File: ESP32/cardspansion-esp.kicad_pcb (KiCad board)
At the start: 2 copper layers, 22 x 30 mm, 5 parts, among them J1 M2-E 2230, Y1 ASE-32.768KHZ

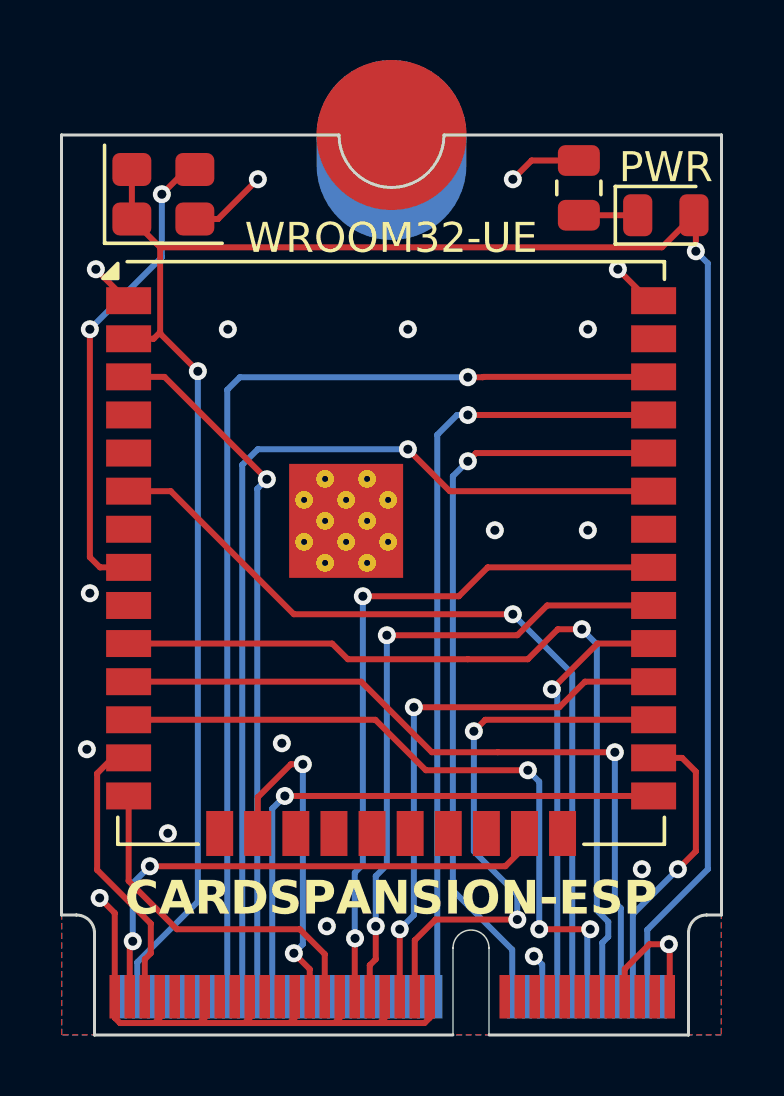
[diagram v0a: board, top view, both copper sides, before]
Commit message: Fix cardspansion-esp I2S wiring
I2S-SDIN and I2S-SDOUT nets were switched around
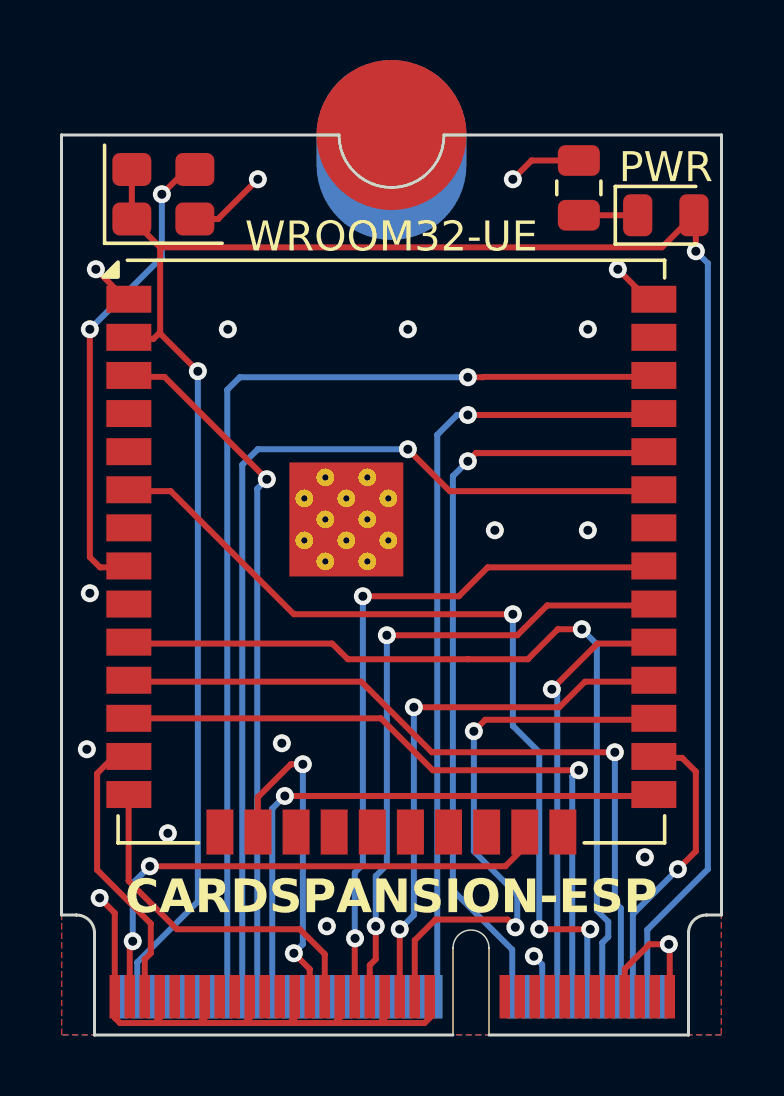
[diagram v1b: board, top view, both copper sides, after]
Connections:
- J1 pad 12: /I2S-SDOUT -> /I2S-SDIN
- J1 pad 14: /I2S-SDIN -> /I2S-SDOUT
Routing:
- net /I2S-SDIN: track 28.1 -> 29.4 mm, vias 1 -> 3
- net /I2S-SDOUT: track 23.5 -> 23.4 mm, vias 3 -> 1
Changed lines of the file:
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@@
 	(footprint "RF_Module:ESP32-WROOM-32UE"
 		(layer "F.Cu")
-		(at 28.4425 38.4575)
+		(at 28.45 38.41)
 		(descr "2.4 GHz Wi-Fi and Bluetooth module, https://www.espressif.com/sites/default/files/documentation/esp32-wroom-32e_esp32-wroom-32ue_datasheet_en.pdf")
 		(tags "2.4 GHz Wi-Fi and Bluetooth module")
@@
 		(sheetname "/")
 		(sheetfile "cardspansion-esp.kicad_sch")
+		(clearance 0.1)
 		(attr smd)
 		(fp_line
@@
 			(layer "F.Fab")
 		)
+		(fp_text user "${REFERENCE}"
+			(at 0 0 0)
+			(unlocked yes)
+			(layer "F.Fab")
+			(effects
+				(font
+					(size 1 1)
+					(thickness 0.15)
+				)
+			)
+		)
 		(pad "1" smd rect
 			(at -8.75 -8.41)
@@
 			(size 0.35 1.45)
 			(layers "B.Cu" "B.Mask")
-			(net 24 "/I2S-SDOUT")
+			(net 55 "/I2S-SDIN")
 			(pinfunction "PCM_IN/I2S_SD_IN")
 			(pintype "input")
@@
 			(size 0.35 1.45)
 			(layers "B.Cu" "B.Mask")
-			(net 55 "/I2S-SDIN")
+			(net 24 "/I2S-SDOUT")
 			(pinfunction "PCM_OUT/I2S_SD_OUT")
 			(pintype "output")
@@
 	)
 	(via
-		(at 36.8 49)
+		(at 18.3 45)
 		(size 0.6)
 		(drill 0.3)
@@
 	)
 	(via
-		(at 18.3 45)
+		(at 36.9 48.6)
 		(size 0.6)
 		(drill 0.3)
@@
 	)
 	(segment
-		(start 27.9175 44.0175)
-		(end 19.6925 44.0175)
-		(width 0.2)
-		(layer "F.Cu")
-		(net 24)
-	)
-	(segment
-		(start 33 45.7)
-		(end 29.6 45.7)
+		(start 29.8329 45.7)
+		(end 34.7 45.7)
 		(width 0.2)
 		(layer "F.Cu")
@@
 	)
 	(segment
-		(start 33.38 51)
-		(end 35.08 51)
+		(start 19.7 43.97)
+		(end 28.1029 43.97)
 		(width 0.2)
 		(layer "F.Cu")
@@
 	)
 	(segment
-		(start 29.6 45.7)
-		(end 27.9175 44.0175)
+		(start 28.1029 43.97)
+		(end 29.8329 45.7)
 		(width 0.2)
 		(layer "F.Cu")
@@
 	)
 	(via
-		(at 33 45.7)
-		(size 0.6)
-		(drill 0.3)
-		(layers "F.Cu" "B.Cu")
-		(net 24)
-	)
-	(via
-		(at 33.38 51)
-		(size 0.6)
-		(drill 0.3)
-		(layers "F.Cu" "B.Cu")
-		(net 24)
-	)
-	(via
-		(at 35.08 51)
+		(at 34.7 45.7)
 		(size 0.6)
 		(drill 0.3)
@@
 	)
 	(segment
-		(start 33.38 51)
-		(end 33.38 46.08)
-		(width 0.2)
-		(layer "B.Cu")
-		(net 24)
-	)
-	(segment
-		(start 33.38 46.08)
-		(end 33 45.7)
+		(start 34.7 45.7)
+		(end 34.68 45.7)
 		(width 0.2)
 		(layer "B.Cu")
@@
 	)
 	(segment
-		(start 35.08 51)
-		(end 34.98 51.1)
+		(start 34.68 45.7)
+		(end 34.48 45.9)
 		(width 0.2)
 		(layer "B.Cu")
@@
 	)
 	(segment
-		(start 34.98 51.1)
-		(end 34.98 53.25)
+		(start 34.48 45.9)
+		(end 34.48 53.25)
 		(width 0.2)
 		(layer "B.Cu")
@@
 	(segment
 		(start 29.8 45.1)
-		(end 32 45.1)
-		(width 0.2)
-		(layer "F.Cu")
-		(net 49)
-	)
-	(segment
-		(start 19.6925 42.7475)
-		(end 27.4475 42.7475)
+		(end 35.9 45.1)
 		(width 0.2)
 		(layer "F.Cu")
@@
 	)
 	(segment
-		(start 28.3 43.6)
+		(start 27.4475 42.7475)
 		(end 29.8 45.1)
 		(width 0.2)
@@
 	)
 	(segment
-		(start 32 45.1)
-		(end 35.9 45.1)
-		(width 0.2)
-		(layer "F.Cu")
-		(net 49)
-	)
-	(segment
-		(start 27.4475 42.7475)
-		(end 28.3 43.6)
+		(start 19.6925 42.7475)
+		(end 27.4475 42.7475)
 		(width 0.2)
 		(layer "F.Cu")
@@
 	)
 	(segment
-		(start 29.23 51.37)
-		(end 29.23 53.25)
+		(start 32.325616 50.677087)
+		(end 29.922913 50.677087)
+		(width 0.2)
+		(layer "F.Cu")
+		(net 53)
+	)
+	(segment
+		(start 32.582711 50.934182)
+		(end 32.325616 50.677087)
 		(width 0.2)
 		(layer "F.Cu")
@@
 	(segment
 		(start 29.922913 50.677087)
-		(end 32.648064 50.677087)
+		(end 29.23 51.37)
 		(width 0.2)
 		(layer "F.Cu")
@@
 	(segment
 		(start 29.23 51.37)
-		(end 29.922913 50.677087)
+		(end 29.23 53.25)
 		(width 0.2)
 		(layer "F.Cu")
@@
 	)
 	(via
-		(at 32.648064 50.677087)
+		(at 32.582711 50.934182)
 		(size 0.6)
 		(drill 0.3)
@@
 	)
 	(segment
-		(start 32.648064 50.677087)
+		(start 32.648064 50.868829)
 		(end 32.648064 49.848064)
 		(width 0.2)
@@
 	)
 	(segment
+		(start 32.582711 50.934182)
+		(end 32.648064 50.868829)
+		(width 0.2)
+		(layer "B.Cu")
+		(net 53)
+	)
+	(segment
 		(start 32.5 40.5)
 		(end 25.2 40.5)
@@
 	)
 	(segment
+		(start 33.38 51)
+		(end 35.08 51)
+		(width 0.2)
+		(layer "F.Cu")
+		(net 55)
+	)
+	(segment
 		(start 25.2 40.5)
 		(end 21.0975 36.3975)
@@
 		(net 55)
 	)
+	(via
+		(at 33.38 51)
+		(size 0.6)
+		(drill 0.3)
+		(layers "F.Cu" "B.Cu")
+		(net 55)
+	)
+	(via
+		(at 35.08 51)
+		(size 0.6)
+		(drill 0.3)
+		(layers "F.Cu" "B.Cu")
+		(net 55)
+	)
+	(segment
+		(start 33.38 45.1)
+		(end 33.38 51)
+		(width 0.2)
+		(layer "B.Cu")
+		(net 55)
+	)
+	(segment
+		(start 35.08 51)
+		(end 34.98 51.1)
+		(width 0.2)
+		(layer "B.Cu")
+		(net 55)
+	)
+	(segment
+		(start 34.98 51.1)
+		(end 34.98 53.25)
+		(width 0.2)
+		(layer "B.Cu")
+		(net 55)
+	)
 	(segment
 		(start 32.5 40.5)
-		(end 34.48 42.48)
+		(end 32.5 44.22)
 		(width 0.2)
 		(layer "B.Cu")
@@
 	)
 	(segment
-		(start 34.48 42.48)
-		(end 34.48 53.25)
+		(start 32.5 44.22)
+		(end 33.38 45.1)
 		(width 0.2)
 		(layer "B.Cu")
